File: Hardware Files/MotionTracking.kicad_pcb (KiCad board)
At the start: 2 copper layers, 1 part, among them U1 LSM6DSV16XTR

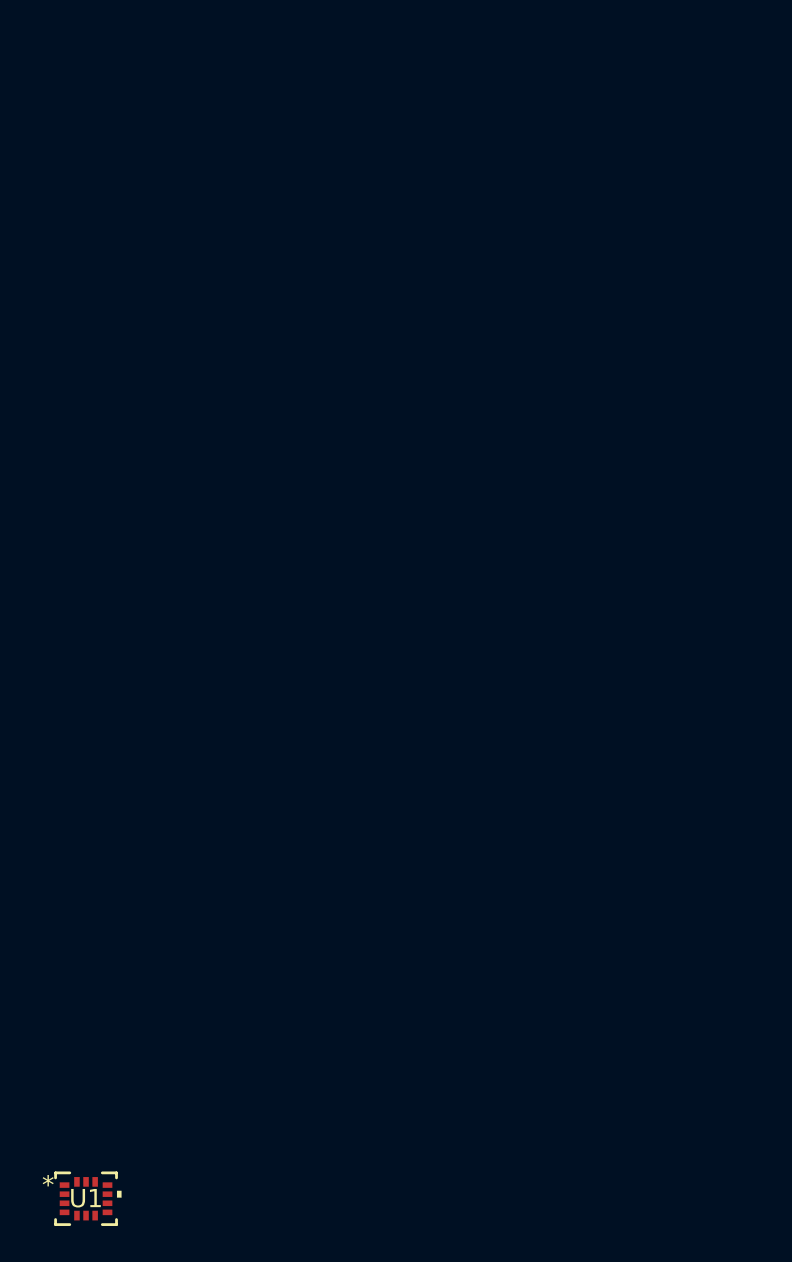
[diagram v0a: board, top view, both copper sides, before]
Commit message: STARTED PCB DESIGN!!
Footprints added to schematic components(some may need to be changed). Organized components and started some rough draft routing. Will most likely need some reorganization, how will parts affect each other(caps, inductors)? NEED TO ADD SOLDER POINTS for battery holder AND FOR 2 other IMUs.
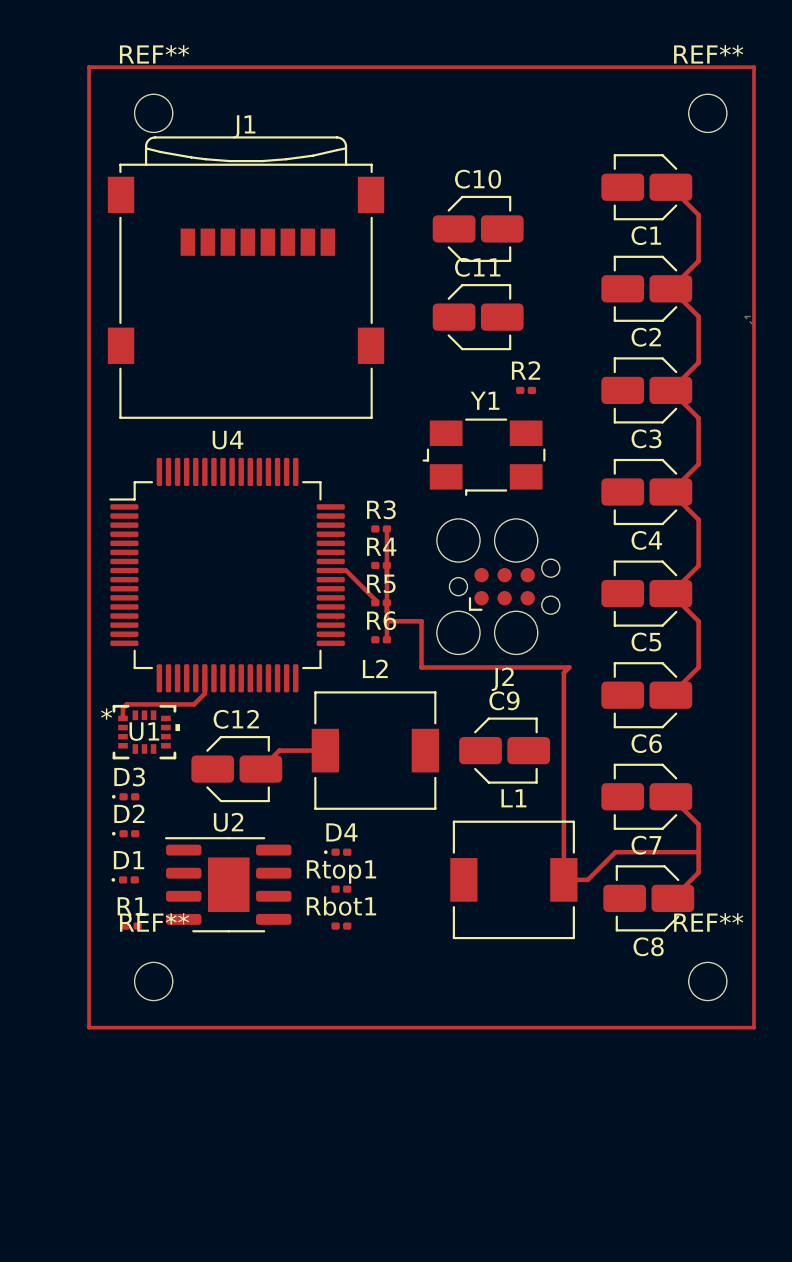
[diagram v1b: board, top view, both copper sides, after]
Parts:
- added C1: 4.7u, Capacitor_SMD:C_Elec_3x5.4, F.Cu at (171.9, 70.6)
- added C10: 2pF, Capacitor_SMD:C_Elec_3x5.4, F.Cu at (162.6, 72.9)
- added C11: 2pF, Capacitor_SMD:C_Elec_3x5.4, F.Cu at (162.6, 77.8)
- added C12: 0.1uF, Capacitor_SMD:C_Elec_3x5.4, F.Cu at (149.4, 102.6)
- added C2: 100nF, Capacitor_SMD:C_Elec_3x5.4, F.Cu at (171.9, 76.2)
- added C3: 100nF, Capacitor_SMD:C_Elec_3x5.4, F.Cu at (171.9, 81.8)
- added C4: 100nF, Capacitor_SMD:C_Elec_3x5.4, F.Cu at (171.9, 87.4)
- added C5: 100nF, Capacitor_SMD:C_Elec_3x5.4, F.Cu at (171.9, 93.0)
- added C6: 100nF, Capacitor_SMD:C_Elec_3x5.4, F.Cu at (171.9, 98.6)
- added C7: 100nF, Capacitor_SMD:C_Elec_3x5.4, F.Cu at (171.9, 104.1)
- added C8: 1uF, Capacitor_SMD:C_Elec_3x5.4, F.Cu at (172.0, 109.7)
- added C9: 47u?, Capacitor_SMD:C_Elec_3x5.4, F.Cu at (164.1, 101.6)
- added D1: D_Schottky, Diode_SMD:D_0201_0603Metric, F.Cu at (143.4, 108.7)
- added D2: D_Schottky, Diode_SMD:D_0201_0603Metric, F.Cu at (143.4, 106.2)
- added D3: D_Schottky, Diode_SMD:D_0201_0603Metric, F.Cu at (143.4, 104.1)
- added D4: D_Schottky, Diode_SMD:D_0201_0603Metric, F.Cu at (155.1, 107.2)
- added J1: Micro_SD_Card_Det1, Connector_Card:microSD_HC_Wuerth_693072010801, F.Cu at (149.9, 75.2)
- added J2: Conn_ST_STDC14, Connector:Tag-Connect_TC2030-IDC-FP_2x03_P1.27mm_Vertical, F.Cu at (164.1, 92.6)
- added L1: 27nH, Inductor_SMD:L_6.3x6.3_H3, F.Cu at (164.6, 108.7)
- added L2: ~1.85uH, Inductor_SMD:L_6.3x6.3_H3, F.Cu at (157.0, 101.6)
- added R1: 3.17M, Resistor_SMD:R_0201_0603Metric, F.Cu at (143.6, 111.3)
- added R2: ??, Resistor_SMD:R_0201_0603Metric, F.Cu at (165.3, 81.8)
- added R3: 10k, Resistor_SMD:R_0201_0603Metric, F.Cu at (157.3, 89.4)
- added R4: 10k, Resistor_SMD:R_0201_0603Metric, F.Cu at (157.3, 91.4)
- added R5: 10k, Resistor_SMD:R_0201_0603Metric, F.Cu at (157.3, 93.5)
- added R6: 10k, Resistor_SMD:R_0201_0603Metric, F.Cu at (157.3, 95.5)
- added REF**: MountingHole_2.1mm, MountingHole:MountingHole_2.1mm, F.Cu at (175.3, 66.5)
- added REF**: MountingHole_2.1mm, MountingHole:MountingHole_2.1mm, F.Cu at (144.8, 114.3)
- added REF**: MountingHole_2.1mm, MountingHole:MountingHole_2.1mm, F.Cu at (144.8, 66.5)
- added REF**: MountingHole_2.1mm, MountingHole:MountingHole_2.1mm, F.Cu at (175.3, 114.3)
- added Rbot1: 10.2k, Resistor_SMD:R_0201_0603Metric, F.Cu at (155.1, 111.3)
- added Rtop1: 31.6k, Resistor_SMD:R_0201_0603Metric, F.Cu at (155.1, 109.2)
- added U2: ADP2302ARDZ-3.3, Package_SO:SOIC-8-1EP_3.9x4.9mm_P1.27mm_EP2.29x3mm, F.Cu at (148.9, 109.0)
- added U4: STM32F411RET6, Package_QFP:LQFP-64_10x10mm_P0.5mm, F.Cu at (148.8, 91.9)
- added Y1: 16MHz, Crystal:Crystal_SMD_0603-4Pin_6.0x3.5mm, F.Cu at (163.1, 85.3)
- moved U1 25.9 mm to (144.3, 100.6)
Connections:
- U1 pad 1: unconnected-(U1-SDO/SA0-Pad1) -> SPI1_MISO
- U1 pad 12: unconnected-(U1-CS-Pad12) -> Net-(U1-CS)
- U1 pad 13: unconnected-(U1-SCL-Pad13) -> SPI1_SCK
- U1 pad 14: unconnected-(U1-SDA-Pad14) -> SPI1_MOSI
- U1 pad 8: unconnected-(U1-VDD-Pad8) -> +3.3V
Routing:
- net +3.3VA: track 0.00 -> 46.4 mm
- net +3.3V: track 0.00 -> 34.3 mm
- net SPI1_MISO: track 0.00 -> 6.24 mm
- net Net-(D4-K): track 0.00 -> 3.97 mm
- net I2C3_SCL: track 0.00 -> 3.28 mm
- added copper zone on B.Cu, net GND
- added copper zone on F.Cu, net GND

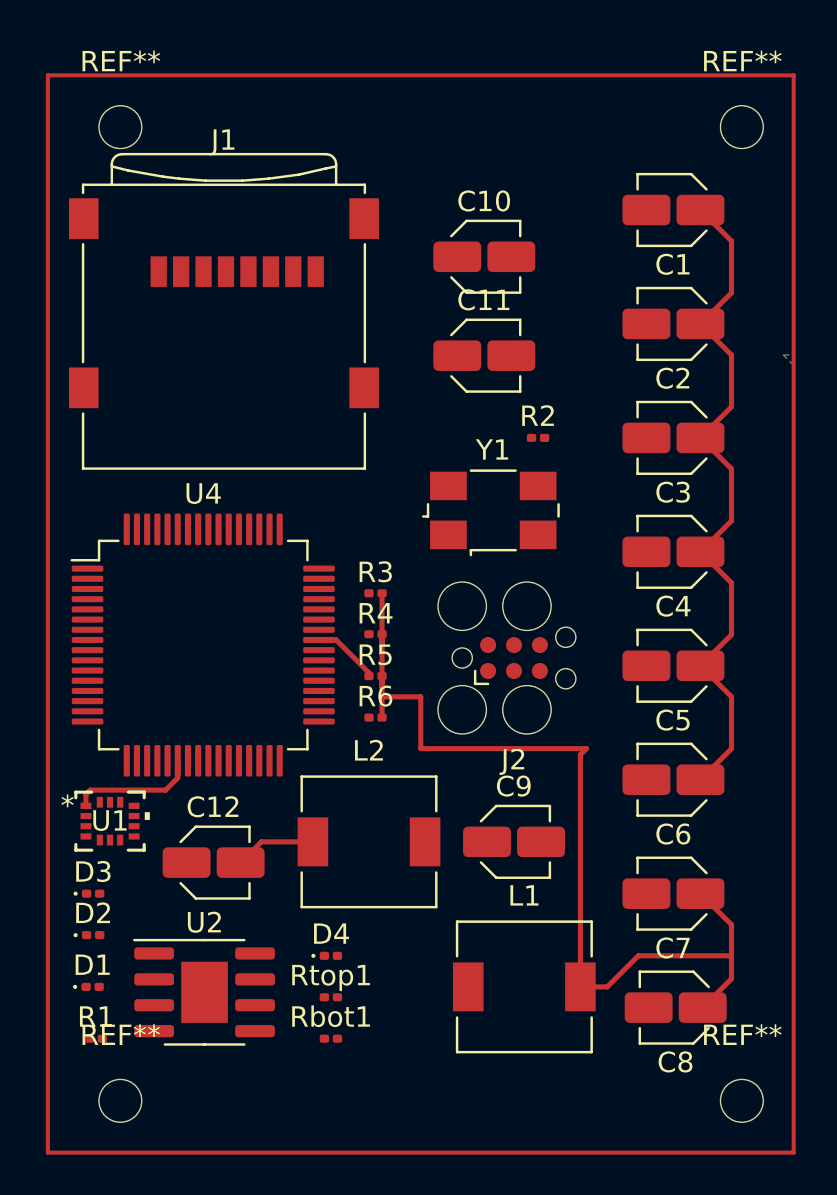
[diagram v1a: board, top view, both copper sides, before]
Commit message: changed footprints and schematic/pcb setup
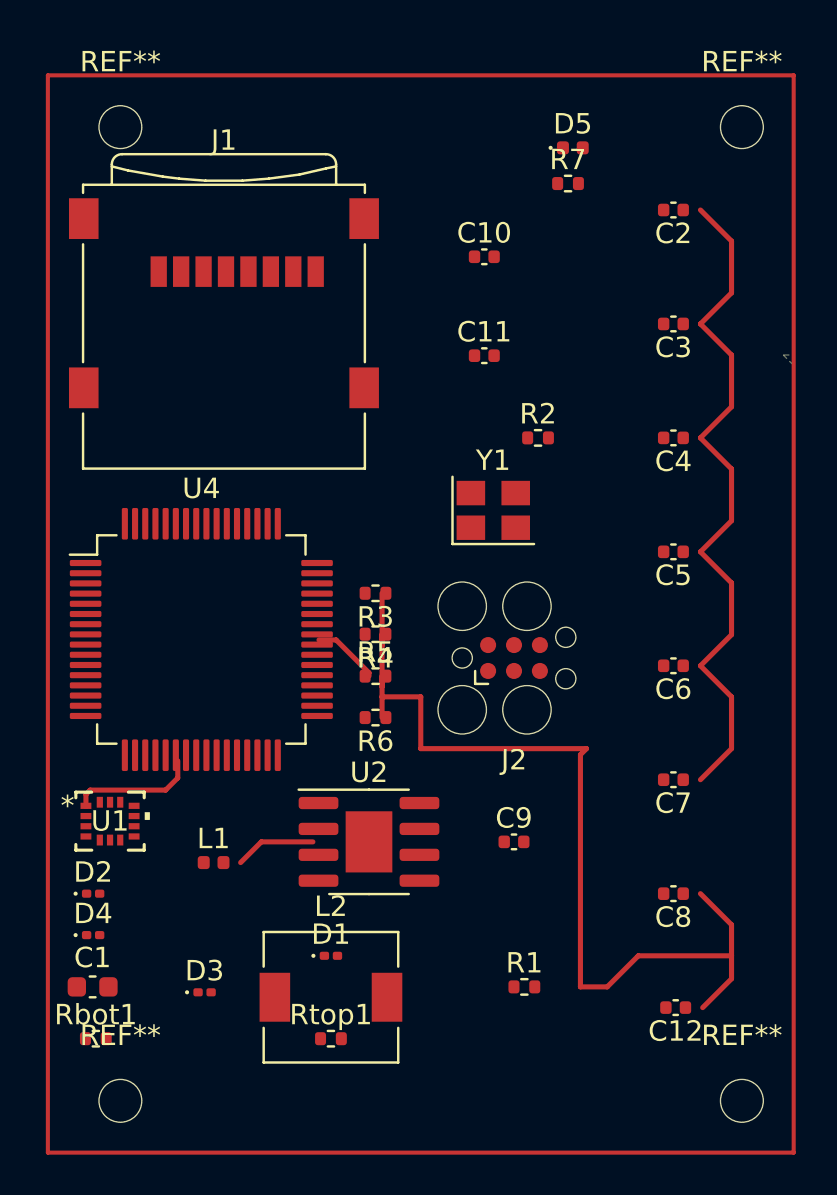
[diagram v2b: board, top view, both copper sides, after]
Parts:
- added D5: LED, LED_SMD:LED_0402_1005Metric, F.Cu at (167.0, 67.6)
- added R7: 220, Resistor_SMD:R_0402_1005Metric, F.Cu at (166.7, 69.3)
- C1: footprint Capacitor_SMD:C_Elec_3x5.4 -> Capacitor_SMD:C_0603_1608Metric
- C10, C11, C12, C2, C3, C4, C5, C6, C7, C8, C9: footprint Capacitor_SMD:C_Elec_3x5.4 -> Capacitor_SMD:C_0402_1005Metric
- L1: footprint Inductor_SMD:L_6.3x6.3_H3 -> Inductor_SMD:L_0402_1005Metric
- R1, R2, R3, R4, R5, R6, Rbot1, Rtop1: footprint Resistor_SMD:R_0201_0603Metric -> Resistor_SMD:R_0402_1005Metric
- Y1: footprint Crystal:Crystal_SMD_0603-4Pin_6.0x3.5mm -> Crystal:Crystal_SMD_3225-4Pin_3.2x2.5mm
- moved C1 47.6 mm to (143.4, 108.7), turned to 0 degrees
- moved C12 23.8 mm to (172.0, 109.7), turned to 180 degrees
- moved R1 21.2 mm to (164.6, 108.7)
- moved L1 16.4 mm to (149.4, 102.6)
- moved D1 11.8 mm to (155.1, 107.2)
- moved D4 11.7 mm to (143.4, 106.2)
- moved Rbot1 11.5 mm to (143.6, 111.3)
- moved U2 10.9 mm to (157.0, 101.6)
- moved L2 7.85 mm to (155.1, 109.2)
- moved D3 7.30 mm to (148.9, 109.0)
- moved C8 5.59 mm to (171.9, 104.1)
- moved C2 5.59 mm to (171.9, 70.6)
- moved C4 5.59 mm to (171.9, 81.8)
- moved C6 5.59 mm to (171.9, 93.0)
- moved C3 5.59 mm to (171.9, 76.2)
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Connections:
- U1 pad 5: unconnected-(U1-VDD_IO-Pad5) -> +3.3V
- U4 pad 8: unconnected-(U4-PC0-Pad8) -> Net-(D5-A)
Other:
- copper layers 2 -> 4
- rule pad_to_mask_clearance: 0 -> 0.08

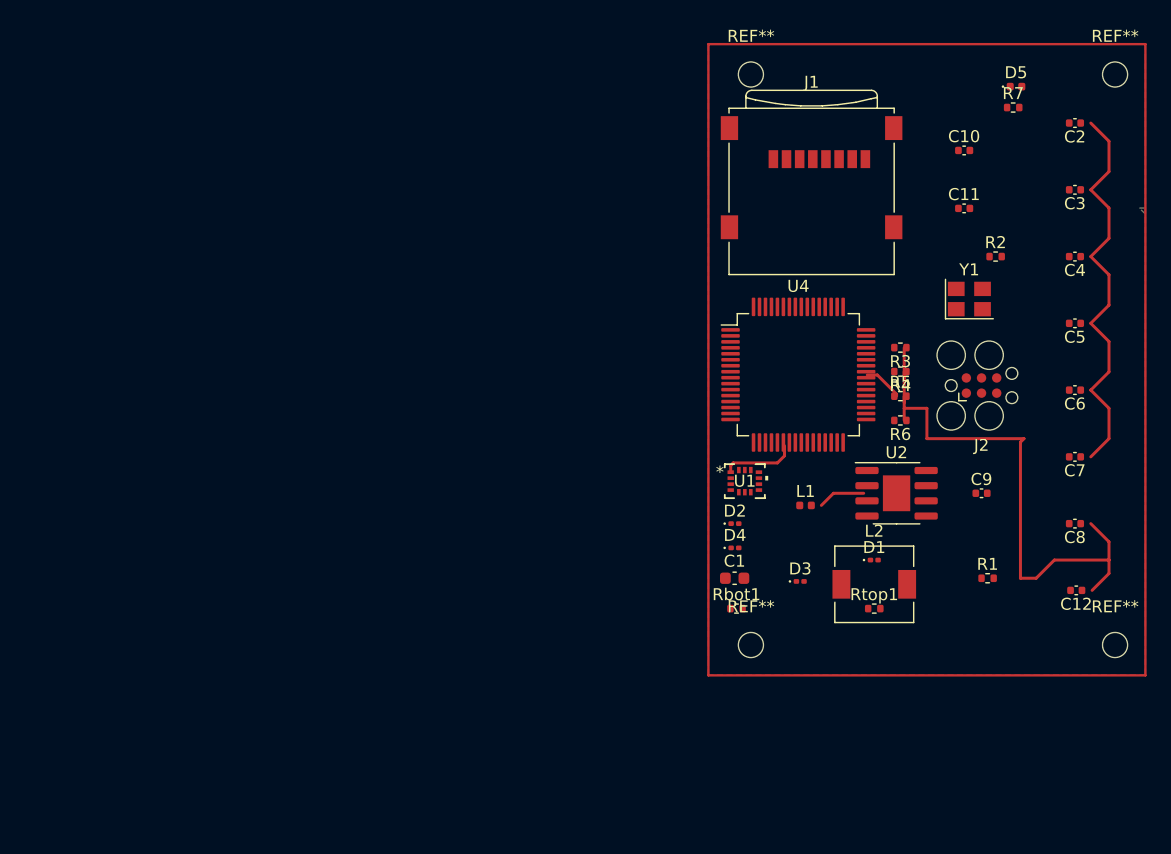
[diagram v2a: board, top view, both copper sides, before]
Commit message: added pinouts for other imus and battery supply. Almost finished layout of pcb, routing next week
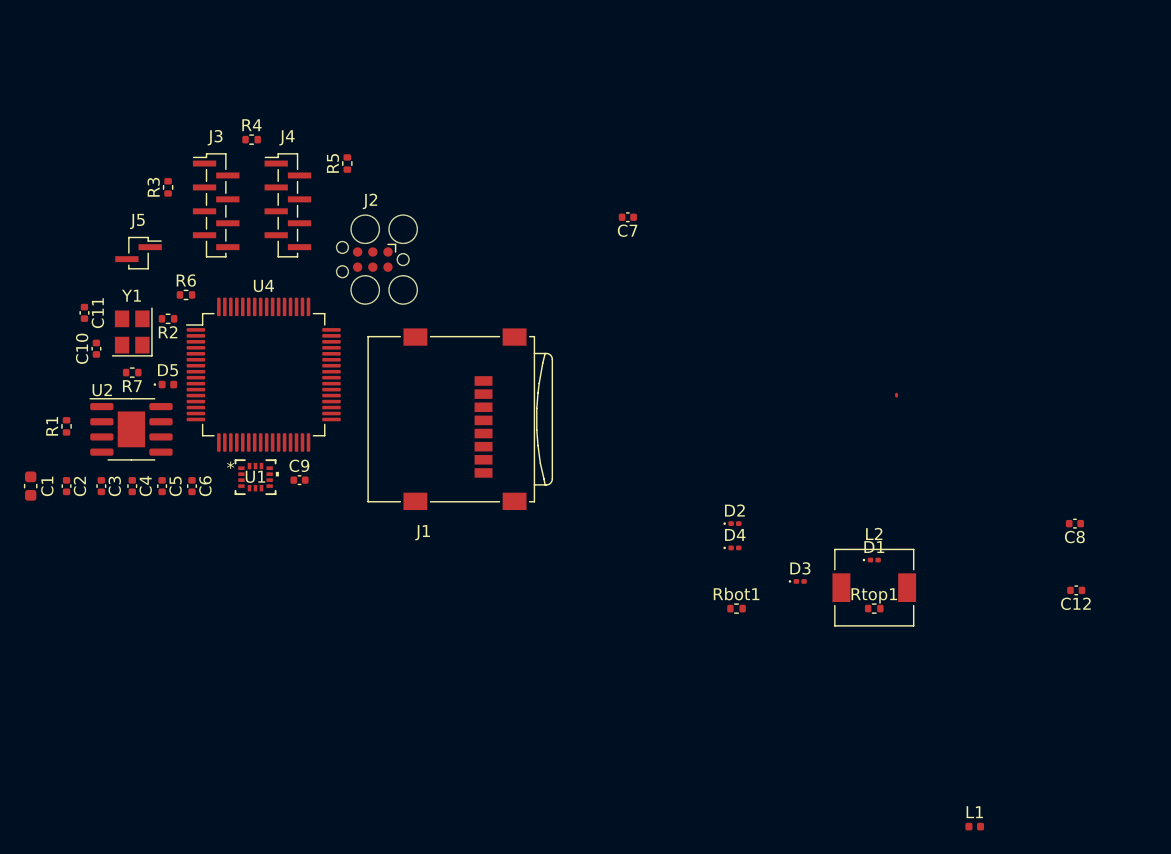
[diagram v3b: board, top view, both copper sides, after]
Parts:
- removed REF** (x4): MountingHole_2.1mm, MountingHole:MountingHole_2.1mm
- added J3: Conn_01x08, Connector_PinSocket_1.00mm:PinSocket_1x08_P1.00mm_Vertical_SMD_Pin1Left, F.Cu at (100.0, 77.5)
- added J4: Conn_01x08, Connector_PinSocket_1.00mm:PinSocket_1x08_P1.00mm_Vertical_SMD_Pin1Left, F.Cu at (106.0, 77.5)
- added J5: Conn_01x02, Connector_PinSocket_1.00mm:PinSocket_1x02_P1.00mm_Vertical_SMD_Pin1Right, F.Cu at (93.5, 81.5)
- moved C2 89.7 mm to (87.5, 101.0), turned to -90 degrees
- moved C3 85.2 mm to (90.4, 101.0), turned to -90 degrees
- moved C4 81.2 mm to (93.0, 101.0), turned to -90 degrees
- moved R1 78.1 mm to (87.5, 96.0), turned to 90 degrees
- moved C5 77.6 mm to (95.5, 101.0), turned to -90 degrees
- moved R7 77.0 mm to (93.0, 91.5), turned to 180 degrees
- moved D5 75.2 mm to (96.0, 92.5)
- moved C10 74.5 mm to (90.0, 89.5), turned to 90 degrees
- moved C6 74.3 mm to (98.0, 101.0), turned to -90 degrees
- moved C11 74.1 mm to (89.0, 86.5), turned to -90 degrees
- moved Y1 70.1 mm to (93.0, 88.1), turned to 90 degrees
- moved R2 69.5 mm to (96.0, 87.0), turned to 180 degrees
- moved U2 64.3 mm to (92.9, 96.2)
- moved R3 62.7 mm to (96.0, 76.0), turned to 90 degrees
- moved R6 60.7 mm to (97.5, 85.0), turned to 0 degrees
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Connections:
- D3 pad 2: Net-(D1-K) -> +BATT
- R1 pad 2: Net-(D1-K) -> +BATT
- U2 pad 2: Net-(D1-K) -> +BATT
- U4 pad 1: unconnected-(U4-VBAT-Pad1) -> +BATT
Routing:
- net +3.3VA: track 46.4 -> 0.00 mm
- net +3.3V: track 34.3 -> 0.00 mm
- net SPI1_MISO: track 6.24 -> 0.00 mm
- net Net-(D4-K): track 3.97 -> 0.00 mm
- net I2C3_SCL: track 3.28 -> 0.16 mm
- removed copper zone on B.Cu, net GND
- removed copper zone on F.Cu, net GND
